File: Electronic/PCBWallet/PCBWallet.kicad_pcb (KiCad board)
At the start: 2 copper layers, 122 x 84 mm, 8 parts, among them U1 NFCTag_ST25DV

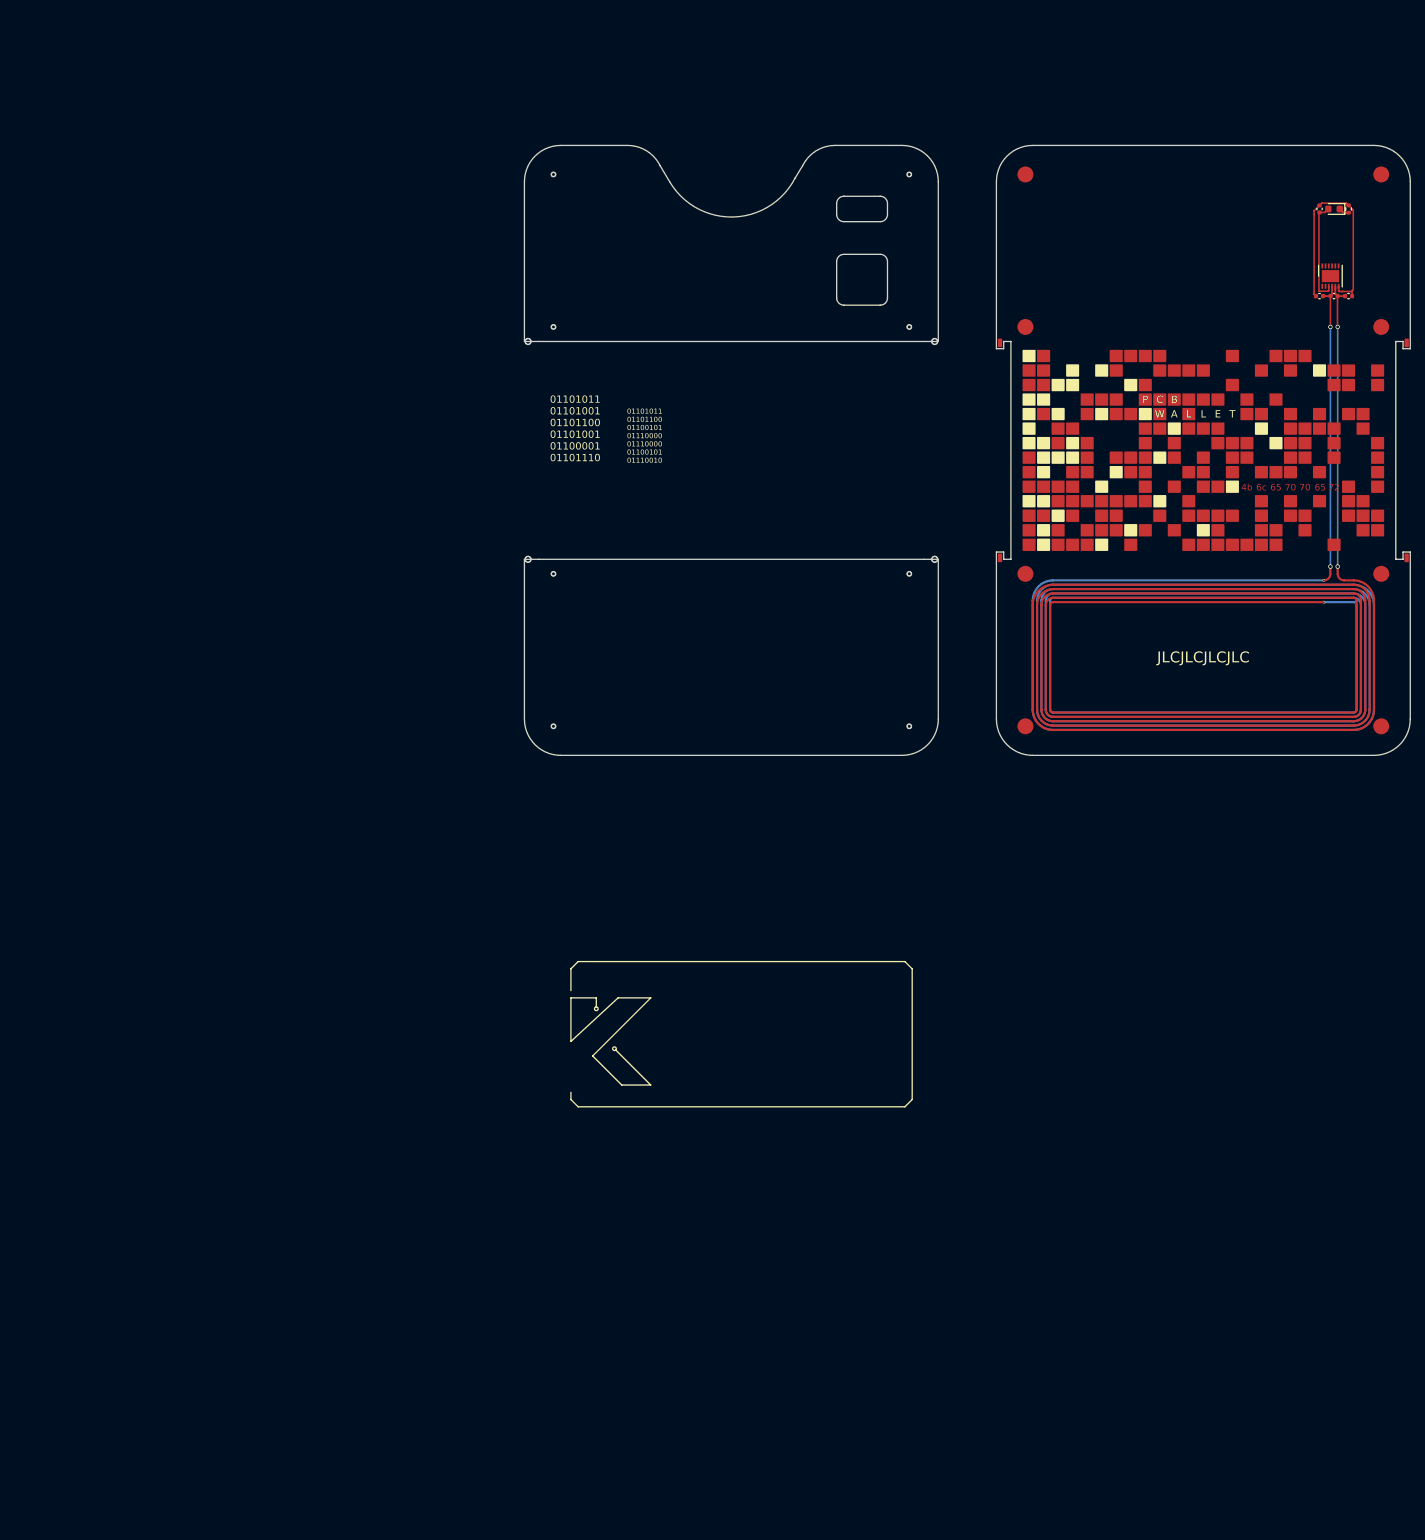
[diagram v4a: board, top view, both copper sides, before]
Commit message: Setup hole wallet with name desing
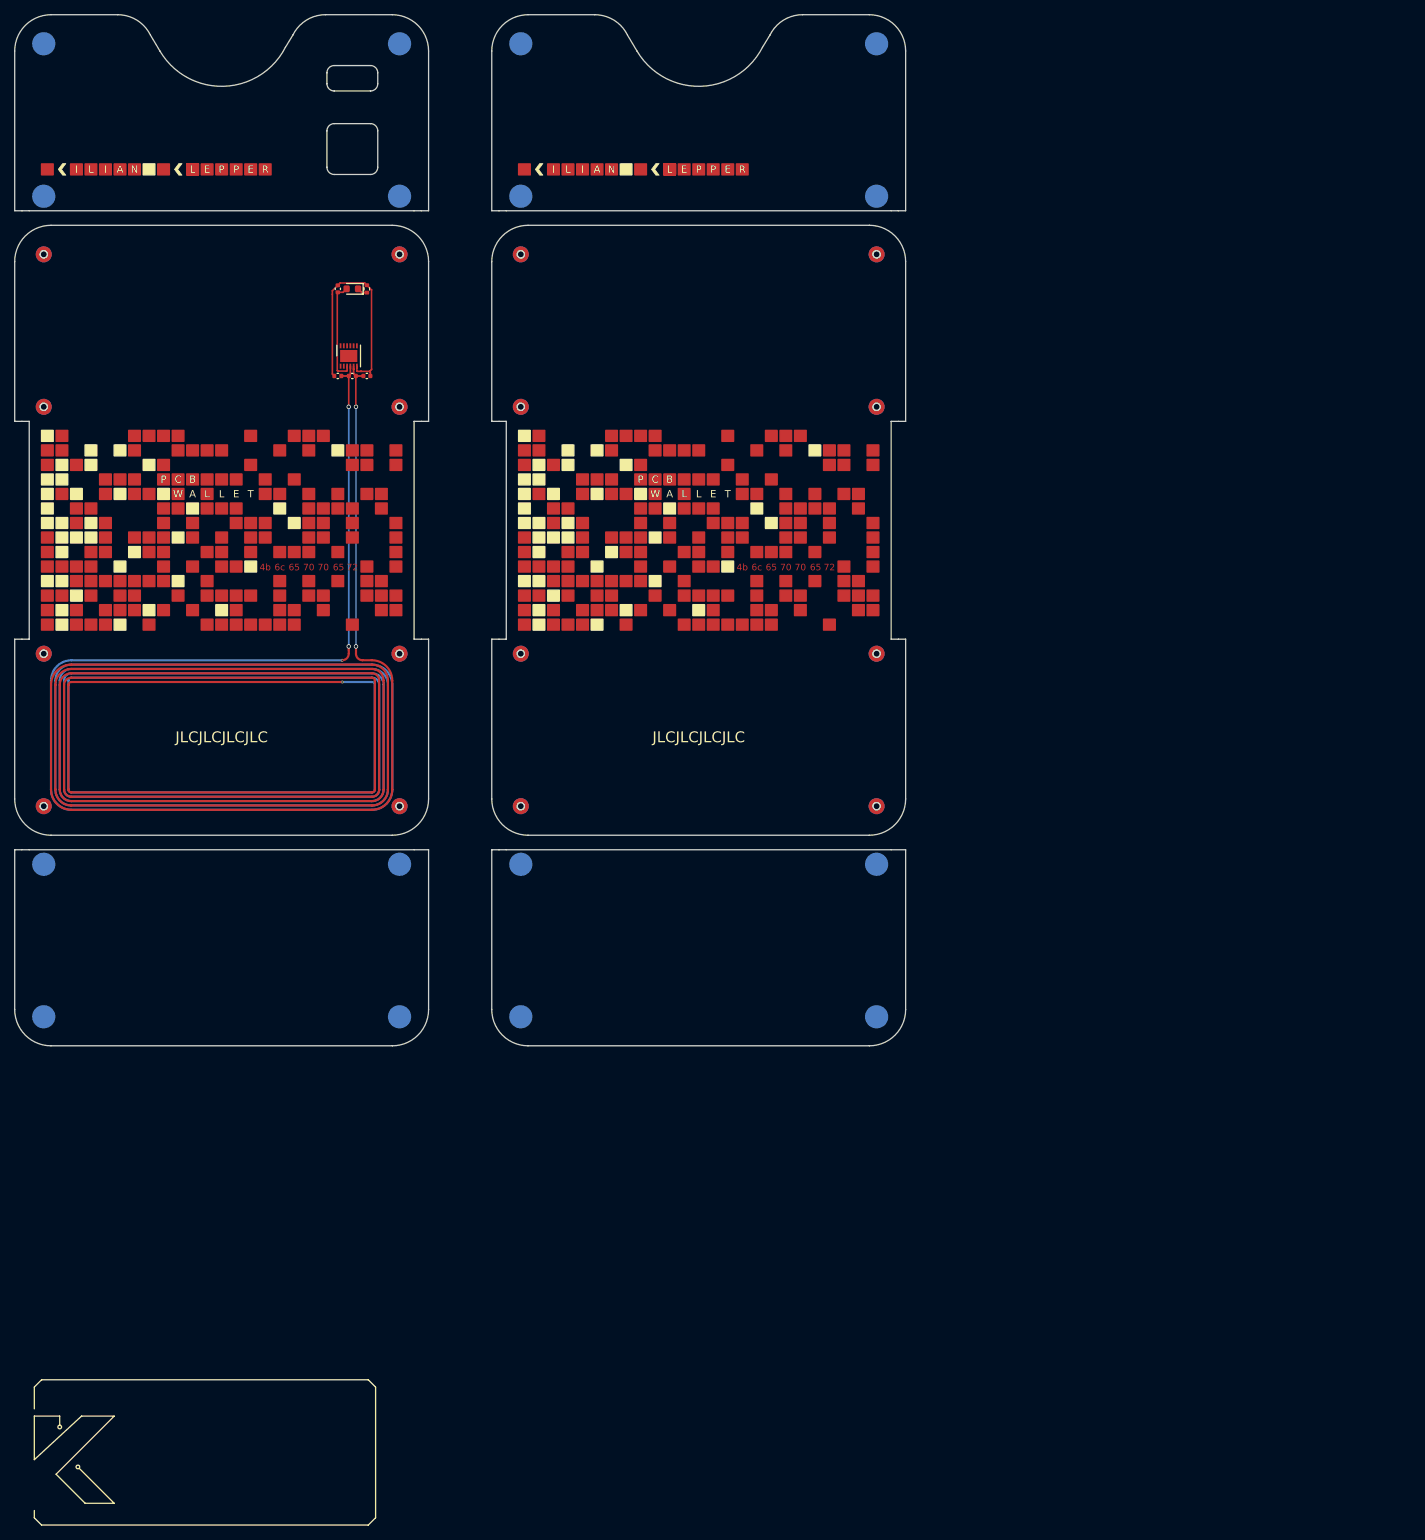
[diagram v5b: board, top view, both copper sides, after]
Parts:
- moved R1 135.6 mm to (78.3, 69.8)
- moved AE1 135.6 mm to (58.3, 131.5)
- moved C1 135.6 mm to (74.3, 81.8)
- moved C2 135.6 mm to (74.3, 69.8)
- moved C3 135.6 mm to (76.3, 81.8)
- moved C4 135.6 mm to (78.3, 81.8)
- moved D1 135.6 mm to (76.3, 69.8)
- moved U1 135.6 mm to (75.8, 79.0)
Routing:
- net (no net): vias 12 -> 16
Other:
- board size 122 x 84 mm -> 122.7 x 142 mm
- board text added: "I"
- board text added: "N"
- board text added: "R"
- board text removed: "01101011 01101001 01101100 01101001 01100001 01101110"
- board text removed: "01101011 01101100 01100101 01110000 01110000 01100101 01110010"
- board text removed: "PCB WALLET"
